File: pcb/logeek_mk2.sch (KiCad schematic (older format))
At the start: 133 parts, among them P1 Power, P10 XH2.54-2P RA, P11 BARREL_JACK, P12 USB_B, P13 DC3 5x2, P14 Power, P15 Analog, P16 Digital, P17 Digital, P2 Analog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

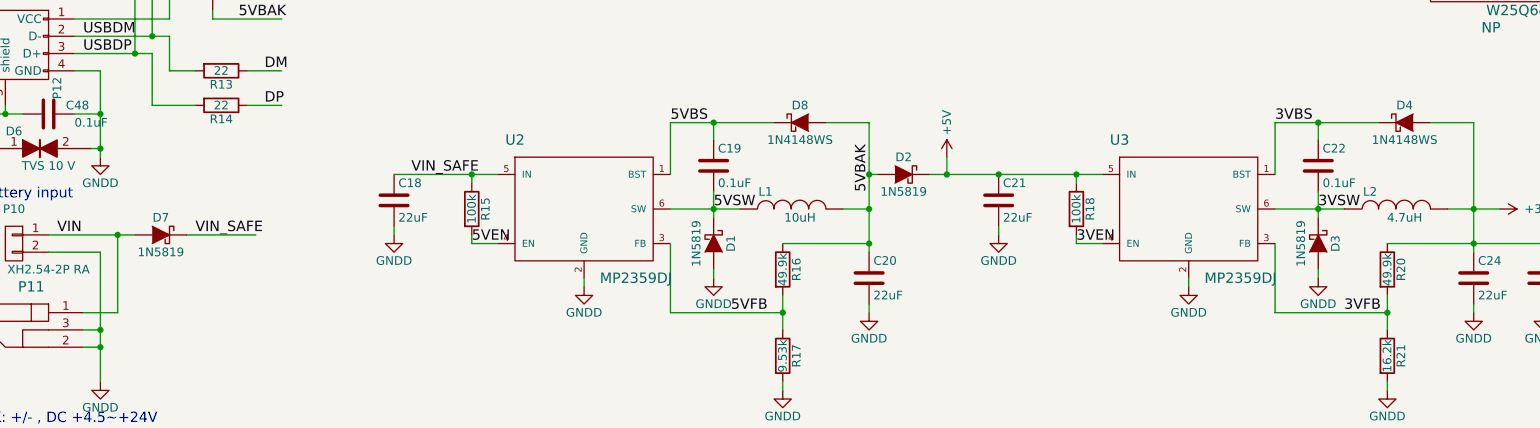
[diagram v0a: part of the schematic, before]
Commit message: Part value update.
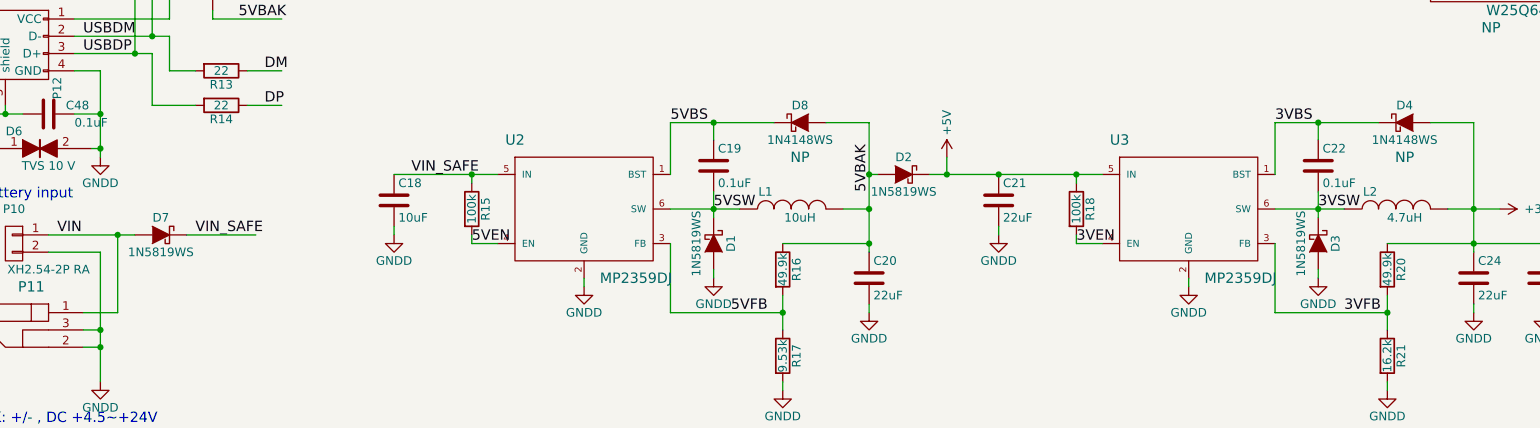
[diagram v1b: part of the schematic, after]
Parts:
- C18: value 22uF -> 10uF
- D1, D2, D3, D7: value 1N5819 -> 1N5819WS
- D4, D8: MOUNT (none) -> NP
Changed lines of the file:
@@
 P 5050 10000
 F 0 "D1" H 5050 10100 50  0000 C CNN
-F 1 "1N5819" H 5050 9900 50  0000 C CNN
+F 1 "1N5819WS" H 5050 9900 50  0000 C CNN
 F 2 "Diodes_SMD:SOD-123" H 5050 10000 60  0001 C CNN
 F 3 "" H 5050 10000 60  0000 C CNN
@@
 P 3200 9750
 F 0 "C18" H 3225 9850 50  0000 L CNN
-F 1 "22uF" H 3225 9650 50  0000 L CNN
+F 1 "10uF" H 3225 9650 50  0000 L CNN
 F 2 "Capacitors_SMD:C_0805" H 3238 9600 30  0001 C CNN
 F 3 "" H 3200 9750 60  0000 C CNN
@@
 P 6150 9600
 F 0 "D2" H 6150 9700 50  0000 C CNN
-F 1 "1N5819" H 6150 9500 50  0000 C CNN
+F 1 "1N5819WS" H 6150 9500 50  0000 C CNN
 F 2 "Diodes_SMD:SOD-123" H 6150 9600 60  0001 C CNN
 F 3 "" H 6150 9600 60  0000 C CNN
@@
 P 8550 10000
 F 0 "D3" H 8550 10100 50  0000 C CNN
-F 1 "1N5819" H 8550 9900 50  0000 C CNN
+F 1 "1N5819WS" H 8550 9900 50  0000 C CNN
 F 2 "Diodes_SMD:SOD-123" H 8550 10000 60  0001 C CNN
 F 3 "" H 8550 10000 60  0000 C CNN
@@
 F 2 "Diodes_SMD:SOD-323" H 9050 9300 60  0001 C CNN
 F 3 "" H 9050 9300 60  0000 C CNN
+F 4 "NP" H 9050 9100 60  0000 C CNN "MOUNT"
 	1    9050 9300
 	1    0    0    -1
@@
 P 1850 9950
 F 0 "D7" H 1850 10050 50  0000 C CNN
-F 1 "1N5819" H 1850 9850 50  0000 C CNN
+F 1 "1N5819WS" H 1850 9850 50  0000 C CNN
 F 2 "Diodes_SMD:SOD-123" H 1850 9950 60  0001 C CNN
 F 3 "" H 1850 9950 60  0000 C CNN
@@
 F 2 "Diodes_SMD:SOD-323" H 5550 9300 60  0001 C CNN
 F 3 "" H 5550 9300 60  0000 C CNN
+F 4 "NP" H 5550 9100 60  0000 C CNN "MOUNT"
 	1    5550 9300
 	1    0    0    -1
@@
 67 0C EF 76 6E 23 A2 28 A3 30 EA 8C 8C EE 29 61 B6 96 F7 23 10 31 20 88 48 22 CE C4 D1 DD 33 A1
 C1 20 90 5B 5F 4D BB 68 21 5B 21 11 51 00 F2 FF 01 E3 1D 24 91 F8 AC 1D 88 00 00 00 00 49 45 4E
-44 AE 42 60 82 75
+44 AE 42 60 82 00
 EndData
 $EndBitmap

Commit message: Corrected FPGA footprint. Delete extra oscillator. Update silkscreen.
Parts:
- removed C13: 0.1uF, Capacitors_SMD:C_0402, symbol C
- removed X1: 25MHz 50ppm, OSC3225, symbol IQXO/7X
- C27, C28, C29, C35, C36, C37, C43, C44, C45: value 0.1uF -> 1nF
- R1, R41: value 220 -> 330
- U1: footprint Housings_QFP:TQFP-144_20x20mm_Pitch0.5mm -> Logeek_MK2:TQFP-144EP_20x20mm_Pitch0.5mm
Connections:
- net labels removed: USERCLK
- wire segments 547 -> 542
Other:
- note added: "(Alaternative)"
- note removed: "Battery input"
- moved on the sheet: C48, D6, D7, P10, P11, P12, P9, Q2, R13, R14

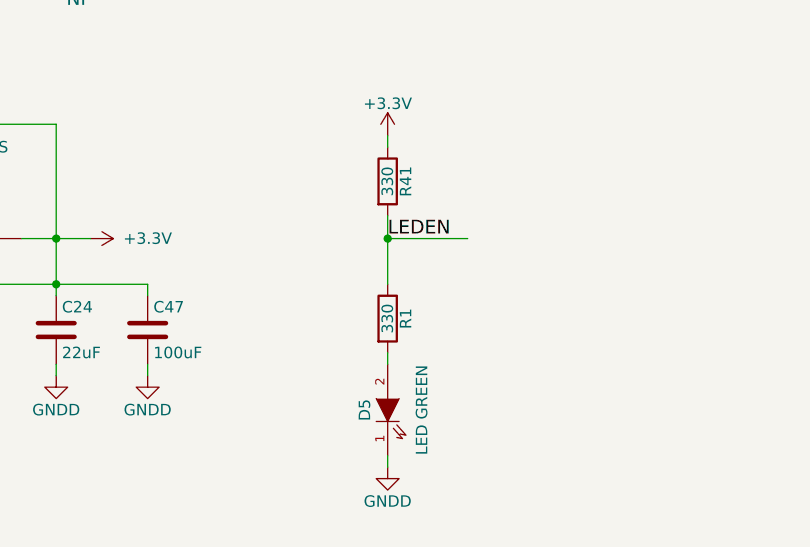
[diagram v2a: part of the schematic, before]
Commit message: Updated socket footprints.
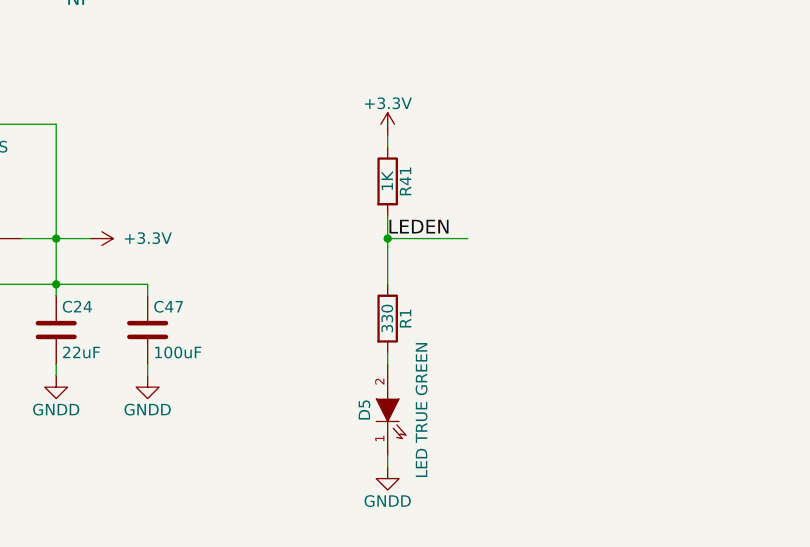
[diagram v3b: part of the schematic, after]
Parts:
- D5: value LED GREEN -> LED TRUE GREEN
- R41: value 330 -> 1K
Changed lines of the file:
@@
 P 10900 10550
 F 0 "D5" H 10900 10650 50  0000 C CNN
-F 1 "LED GREEN" H 10900 10400 50  0000 C CNN
+F 1 "LED TRUE GREEN" H 10900 10400 50  0000 C CNN
 F 2 "LEDs:LED-0603" H 10900 10550 60  0001 C CNN
 F 3 "" H 10900 10550 60  0000 C CNN
@@
 P 10900 9550
 F 0 "R41" V 10980 9550 50  0000 C CNN
-F 1 "330" V 10900 9550 50  0000 C CNN
+F 1 "1K" V 10900 9550 50  0000 C CNN
 F 2 "Resistors_SMD:R_0402_HandSoldering" V 10830 9550 30  0001 C CNN
 F 3 "" H 10900 9550 30  0000 C CNN
@@
 67 0C EF 76 6E 23 A2 28 A3 30 EA 8C 8C EE 29 61 B6 96 F7 23 10 31 20 88 48 22 CE C4 D1 DD 33 A1
 C1 20 90 5B 5F 4D BB 68 21 5B 21 11 51 00 F2 FF 01 E3 1D 24 91 F8 AC 1D 88 00 00 00 00 49 45 4E
-44 AE 42 60 82 00
+44 AE 42 60 82 9E
 EndData
 $EndBitmap
@@
 00 39 19 59 AF 35 42 7E F6 69 BC 65 B4 12 E9 FA 23 84 AE 83 6F 0F D1 9A 40 57 B7 F2 6C 29 EA 3A
 9E 6A A1 85 FF 38 9C BE D1 9C BA 77 9F E3 4F 15 EE 64 AF AB 31 A7 47 CD F6 48 3D E9 C1 75 26 7B
-81 F3 EA B7 E7 8B FF 0F 20 F4 78 B9 DD 14 EB 4B 00 00 00 00 49 45 4E 44 AE 42 60 82 36
+81 F3 EA B7 E7 8B FF 0F 20 F4 78 B9 DD 14 EB 4B 00 00 00 00 49 45 4E 44 AE 42 60 82 FE
 EndData
 $EndBitmap

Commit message: Footprints update.
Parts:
- C47: footprint Capacitors_SMD:c_elec_4x5.8 -> Logeek_MK2:TantalC_SizeB_EIA-3528_HandSoldering
- D5: footprint LEDs:LED-0603 -> Logeek_MK2:LED-0603
- D6: footprint Resistors_SMD:R_0603_HandSoldering -> Logeek_MK2:R_0402_HandSoldering
- X2: footprint Crystals_Oscillators_SMD:crystal_FA238-TSX3225 -> Logeek_MK2:XTAL3225
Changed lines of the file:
@@
 F 0 "X2" H 11000 5640 50  0000 C CNN
 F 1 "24MHz 50ppm" V 11250 5150 50  0000 L CNN
-F 2 "Crystals_Oscillators_SMD:crystal_FA238-TSX3225" H 11000 5550 60  0001 C CNN
+F 2 "Logeek_MK2:XTAL3225" H 11000 5550 60  0001 C CNN
 F 3 "" H 11000 5550 60  0000 C CNN
 	1    11000 5550
@@
 F 0 "D5" H 10900 10650 50  0000 C CNN
 F 1 "LED TRUE GREEN" H 10900 10400 50  0000 C CNN
-F 2 "LEDs:LED-0603" H 10900 10550 60  0001 C CNN
+F 2 "Logeek_MK2:LED-0603" H 10900 10550 60  0001 C CNN
 F 3 "" H 10900 10550 60  0000 C CNN
 	1    10900 10550
@@
 F 0 "C47" H 9875 10300 50  0000 L CNN
 F 1 "100uF" H 9875 10100 50  0000 L CNN
-F 2 "Capacitors_SMD:c_elec_4x5.8" H 9888 10050 30  0001 C CNN
+F 2 "Logeek_MK2:TantalC_SizeB_EIA-3528_HandSoldering" H 9888 10050 30  0001 C CNN
 F 3 "" H 9850 10200 60  0000 C CNN
 	1    9850 10200
@@
 F 0 "D6" H 1150 9200 50  0000 C CNN
 F 1 "TVS 10 V" H 1350 9000 50  0000 C CNN
-F 2 "Resistors_SMD:R_0603_HandSoldering" H 1300 9100 60  0001 C CNN
+F 2 "Logeek_MK2:R_0402_HandSoldering" H 1300 9100 60  0001 C CNN
 F 3 "" H 1300 9100 60  0000 C CNN
 	1    1300 9100
@@
 67 0C EF 76 6E 23 A2 28 A3 30 EA 8C 8C EE 29 61 B6 96 F7 23 10 31 20 88 48 22 CE C4 D1 DD 33 A1
 C1 20 90 5B 5F 4D BB 68 21 5B 21 11 51 00 F2 FF 01 E3 1D 24 91 F8 AC 1D 88 00 00 00 00 49 45 4E
-44 AE 42 60 82 9E
+44 AE 42 60 82 90
 EndData
 $EndBitmap
@@
 00 39 19 59 AF 35 42 7E F6 69 BC 65 B4 12 E9 FA 23 84 AE 83 6F 0F D1 9A 40 57 B7 F2 6C 29 EA 3A
 9E 6A A1 85 FF 38 9C BE D1 9C BA 77 9F E3 4F 15 EE 64 AF AB 31 A7 47 CD F6 48 3D E9 C1 75 26 7B
-81 F3 EA B7 E7 8B FF 0F 20 F4 78 B9 DD 14 EB 4B 00 00 00 00 49 45 4E 44 AE 42 60 82 FE
+81 F3 EA B7 E7 8B FF 0F 20 F4 78 B9 DD 14 EB 4B 00 00 00 00 49 45 4E 44 AE 42 60 82 89
 EndData
 $EndBitmap

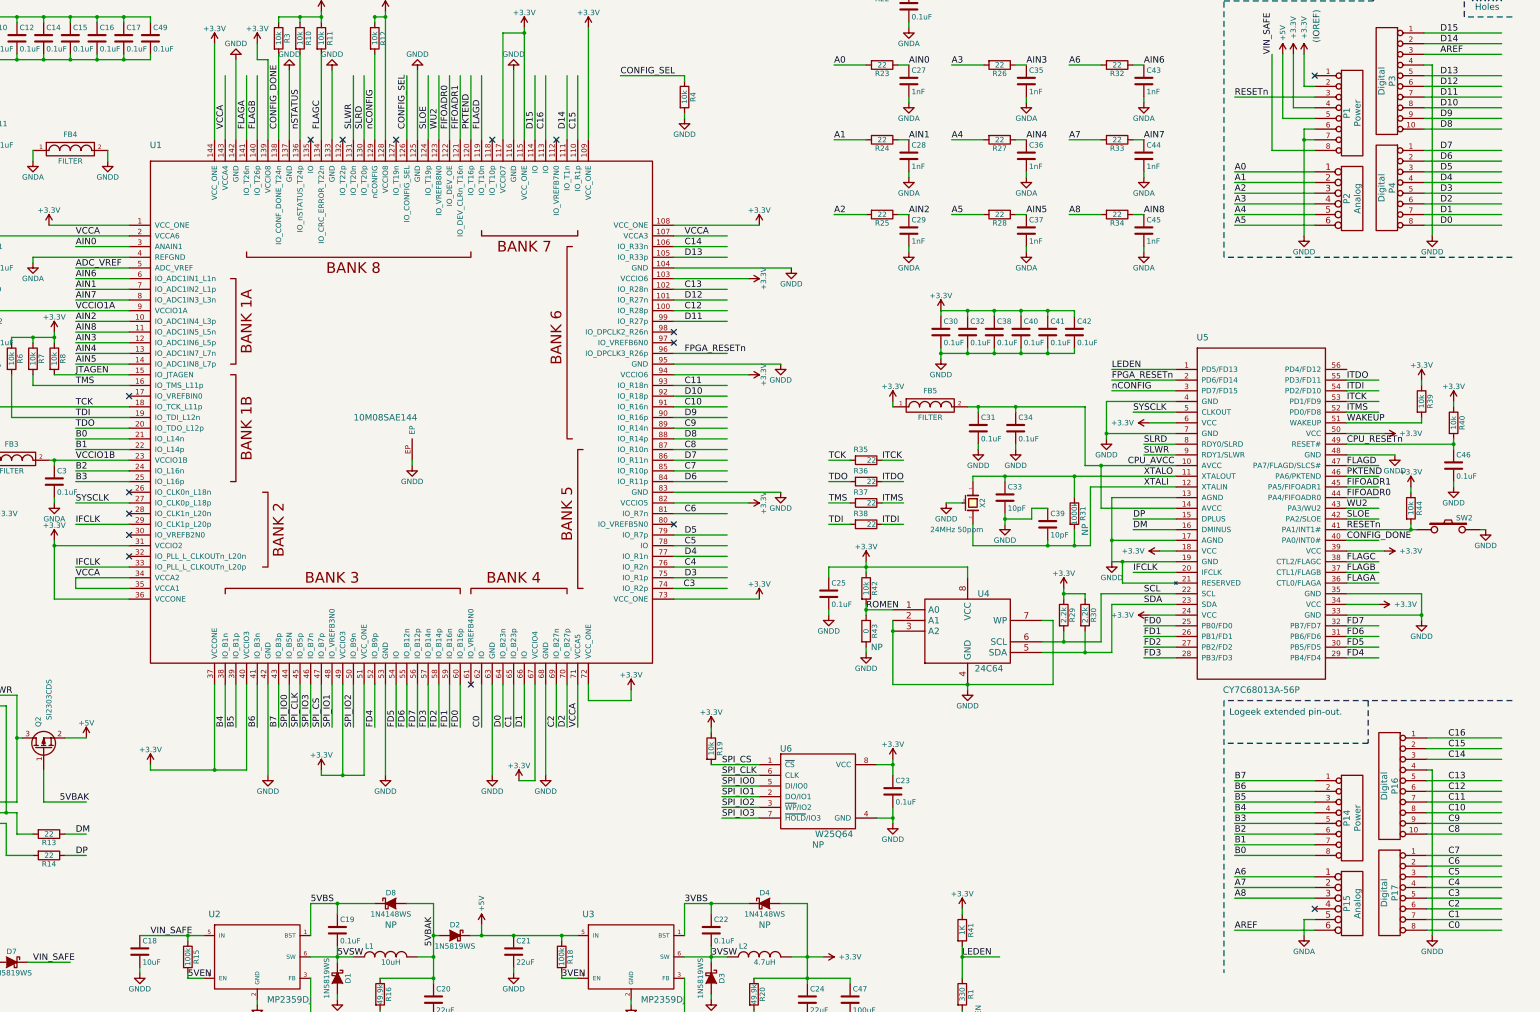
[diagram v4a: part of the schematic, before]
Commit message: Add EXTCLK.
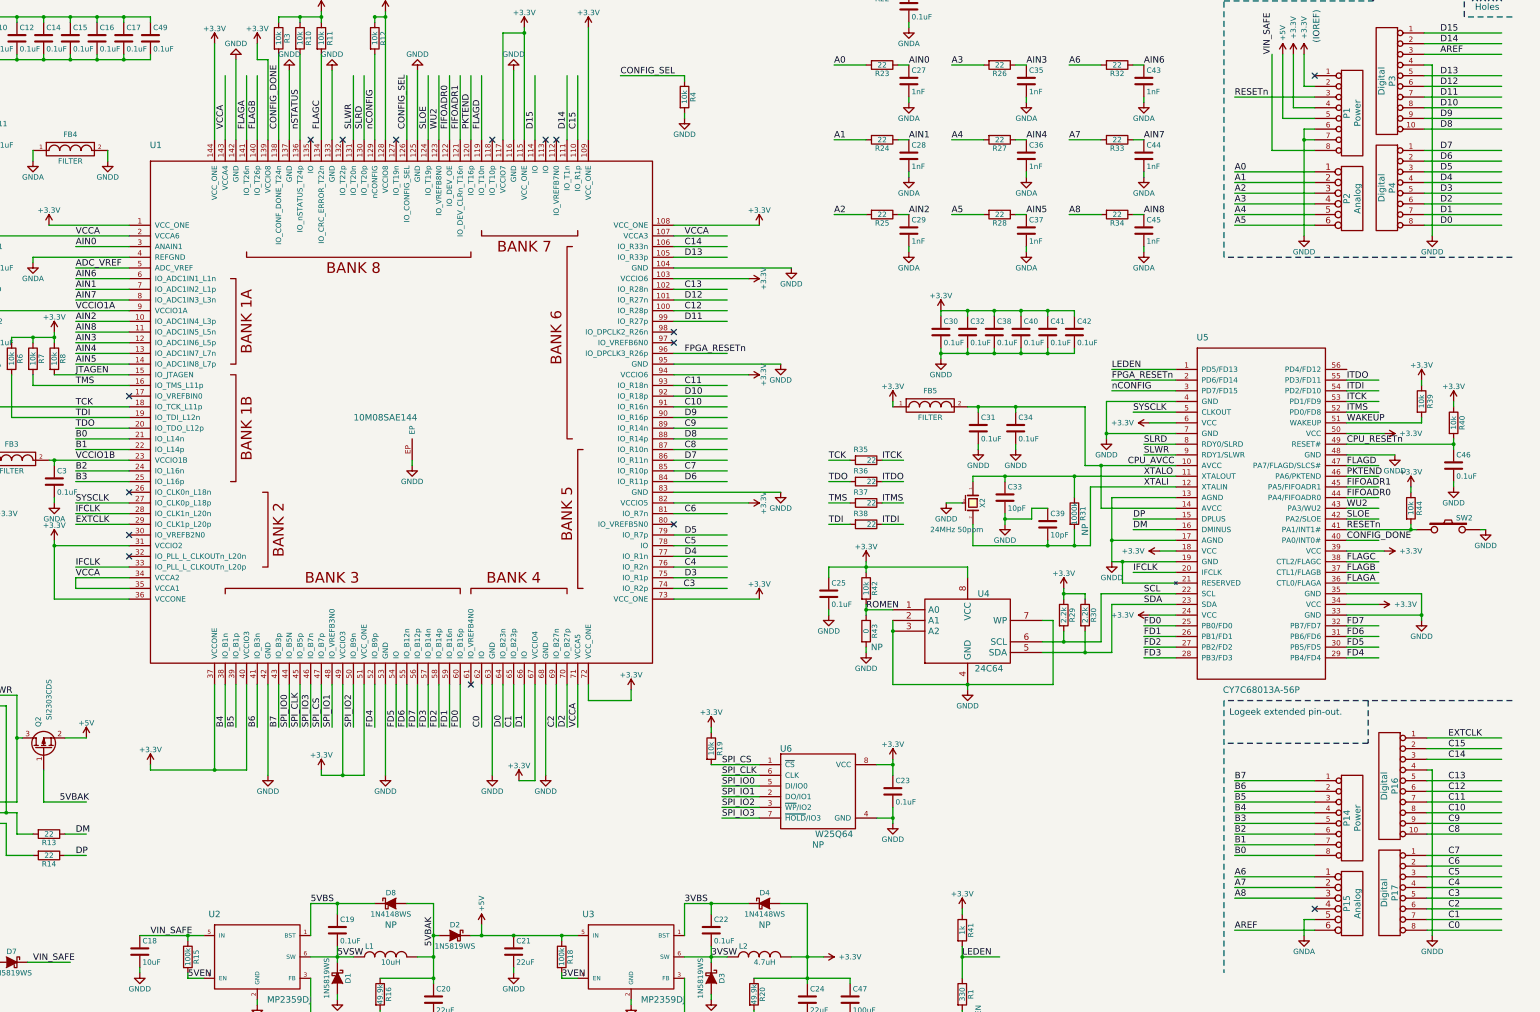
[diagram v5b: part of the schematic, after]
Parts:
- R41: value 1K -> 1k
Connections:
- net labels added: EXTCLK
- net labels removed: C16
